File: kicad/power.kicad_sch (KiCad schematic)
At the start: 76 parts, among them U1 MIMXRT1171DVMAB, U8 TPS62086, U9 TPS62825, Y3 24MHz, Y4 32.768kHz

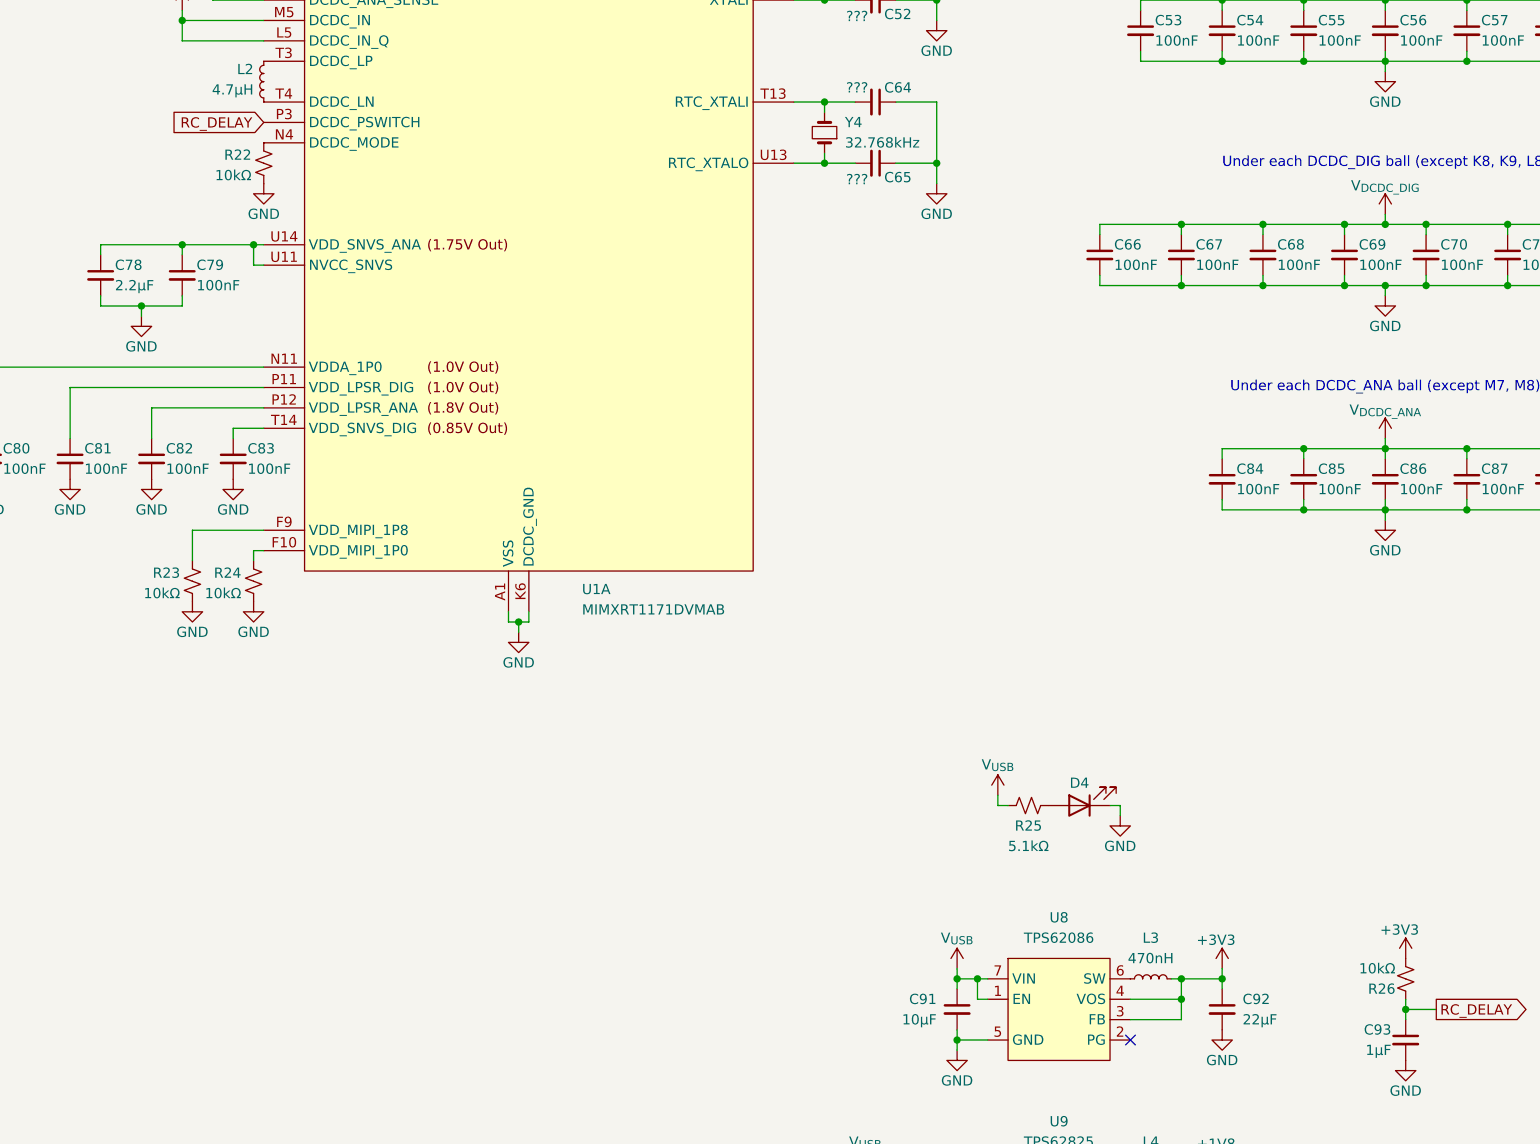
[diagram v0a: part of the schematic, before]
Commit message: added several footprints
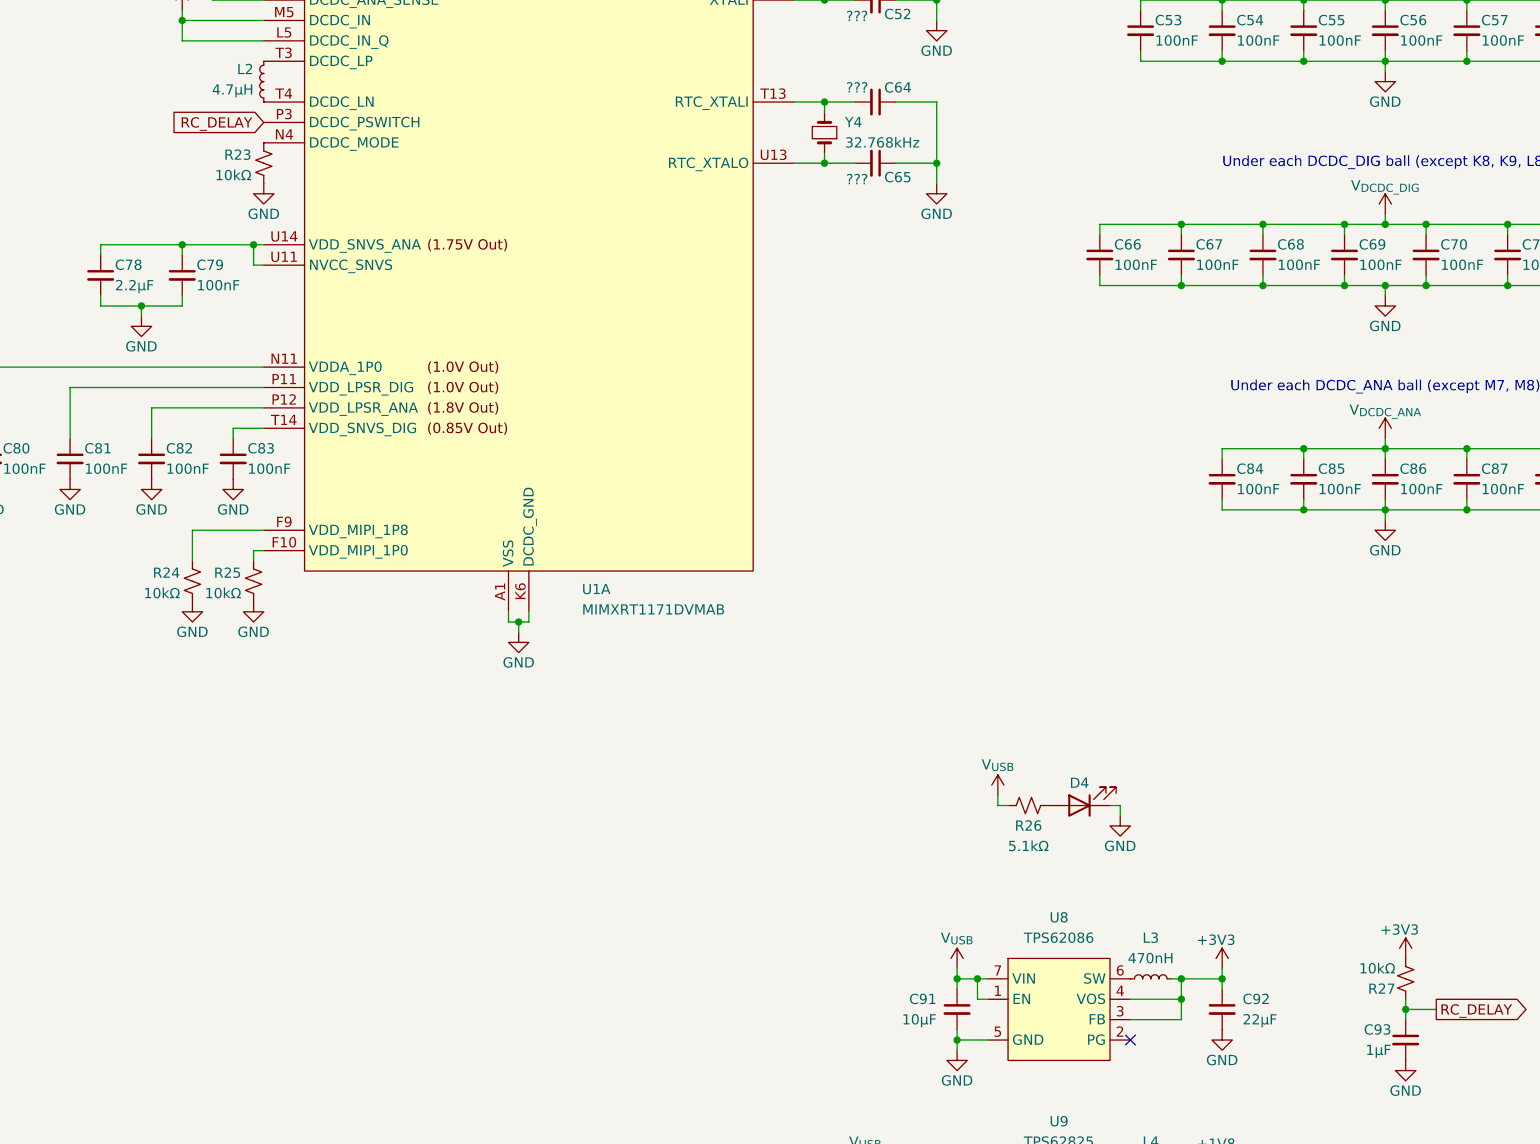
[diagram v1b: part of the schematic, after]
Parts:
- C37, C38, C39, C40, C41, C42, C43, C44, C45, C46, C53, C54, C55, C56, C57, C58, C59, C66, C67, C68, C69, C70, C71, C72, C73, C79, C80, C81, C82, C83, C84, C85, C86, C87, C88: footprint (none) -> Capacitor_SMD:C_0201_0603Metric
- C47, C48, C49, C50, C60, C61, C62, C63, C74, C75, C76, C77, C89, C90, C91: footprint (none) -> Capacitor_SMD:C_0402_1005Metric
- D4: footprint (none) -> LED_SMD:LED_0603_1608Metric
- R23: renamed from R22; footprint (none) -> Resistor_SMD:R_0201_0603Metric
- R24: renamed from R23; footprint (none) -> Resistor_SMD:R_0201_0603Metric
- R25: renamed from R24; footprint (none) -> Resistor_SMD:R_0201_0603Metric
- R26: renamed from R25; footprint (none) -> Resistor_SMD:R_0201_0603Metric
- R27: renamed from R26; footprint (none) -> Resistor_SMD:R_0201_0603Metric
- U1: footprint Package_BGA:MAPBGA-289_14x14mm_Layout17x17_P0.8mm -> project_footprints:MIMXRT1171DVMAB
- U8: footprint (none) -> project_footprints:TPS62086
- U9: footprint (none) -> project_footprints:TPS62825

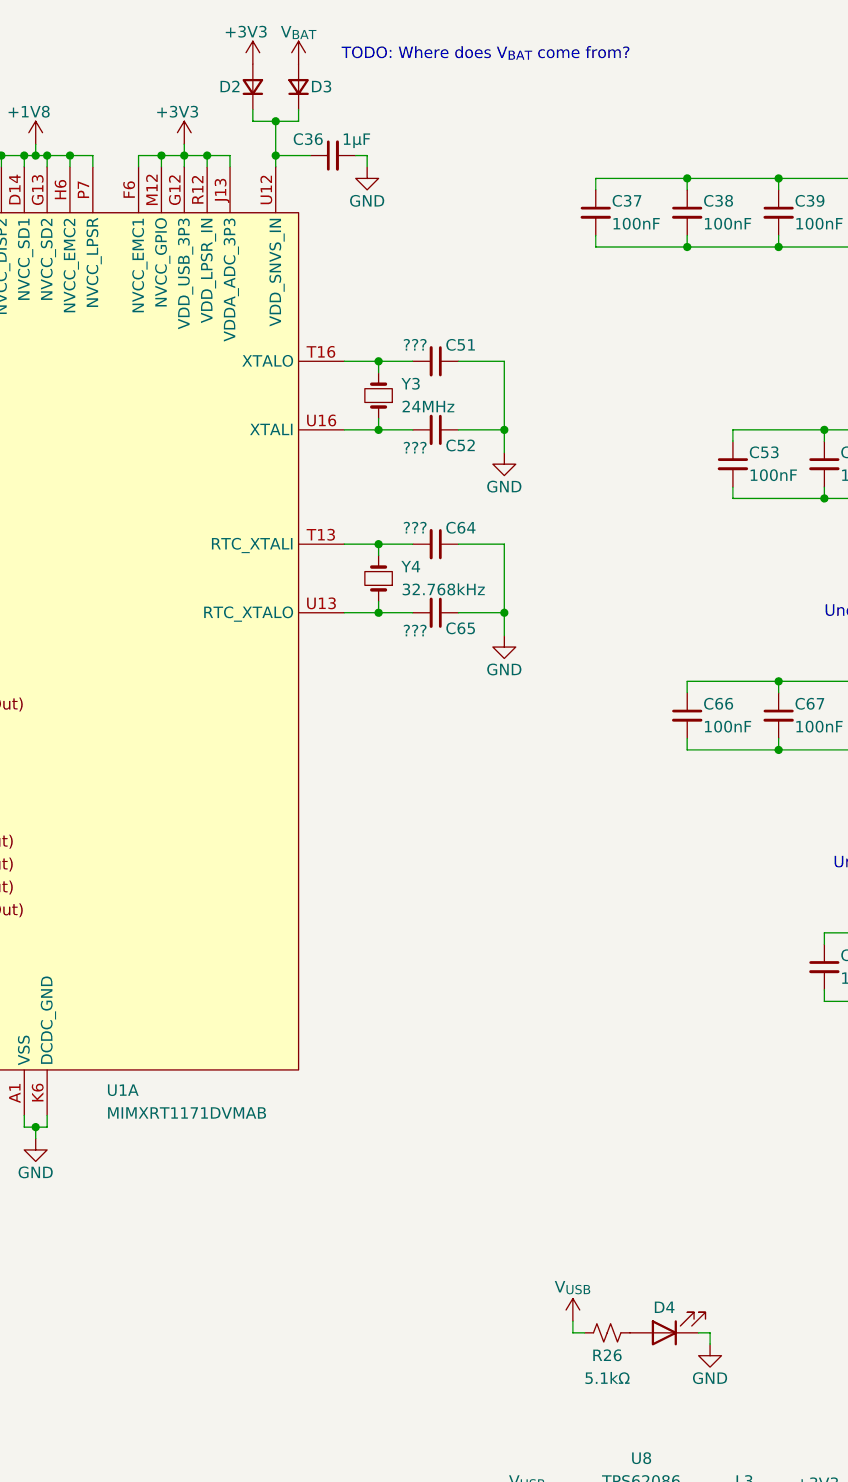
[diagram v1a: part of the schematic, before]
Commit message: added RTC battery connector
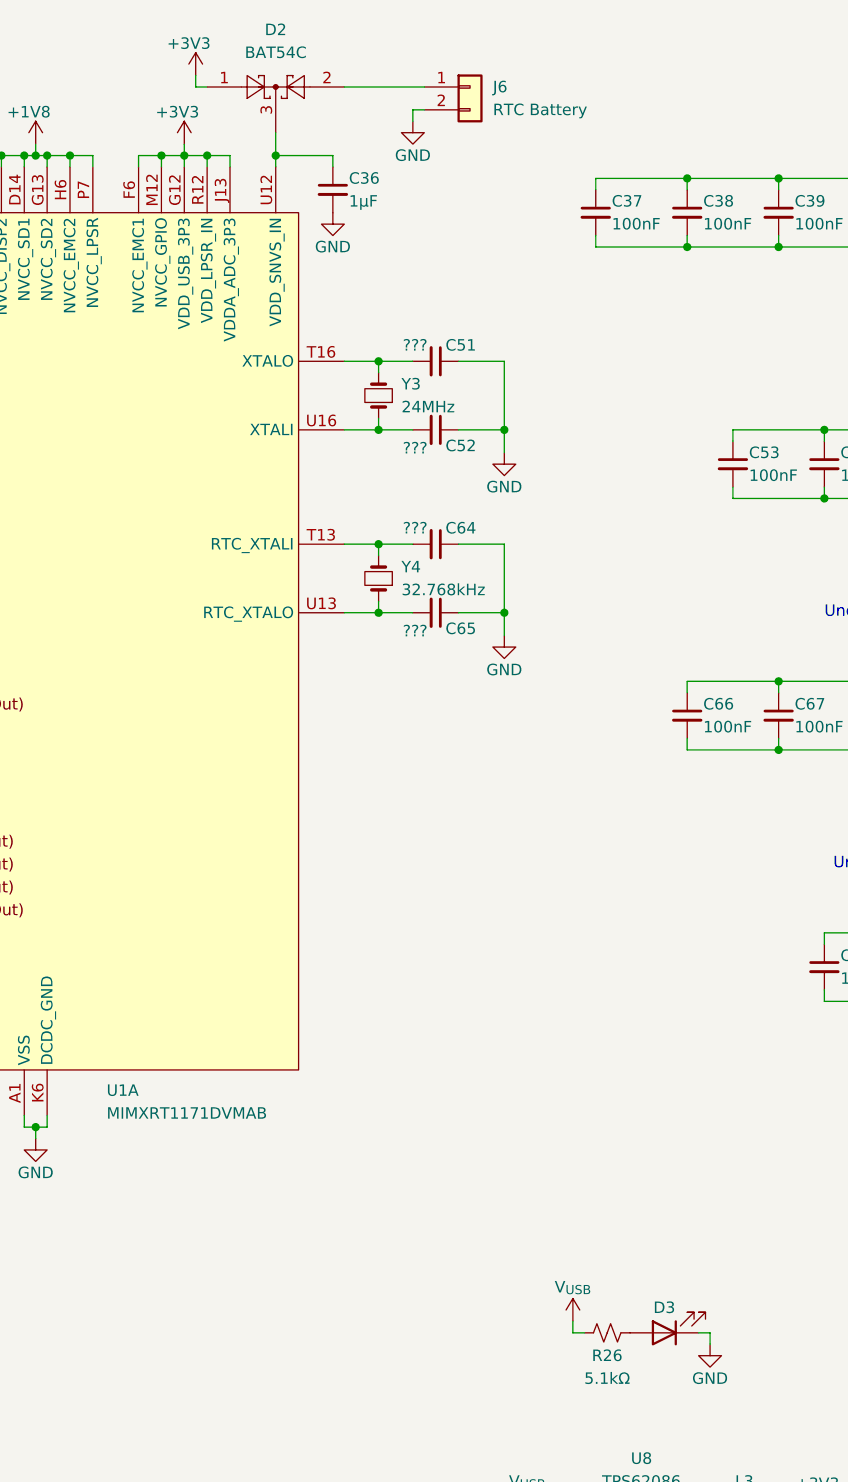
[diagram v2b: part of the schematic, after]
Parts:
- removed D2, D3: ???, symbol Device:D_Small
- added D2: BAT54C, Package_TO_SOT_SMD:SOT-23, symbol Diode:BAT54C
- added J6: RTC Battery, project_footprints:Header-1x02, symbol Connector_Generic:Conn_01x02
- C36: footprint (none) -> Capacitor_SMD:C_0402_1005Metric
- renumbered D4 to D3
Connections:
- net +3V3: now also D2.1
- net GND: now also J6.2 (Pin_2)
- net at C36.1, U1.U12 (VDD_SNVS_IN): now also D2.3
- new net: D2.2, J6.1 (Pin_1)
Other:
- note removed: "TODO: Where does V_{BAT} come from?"

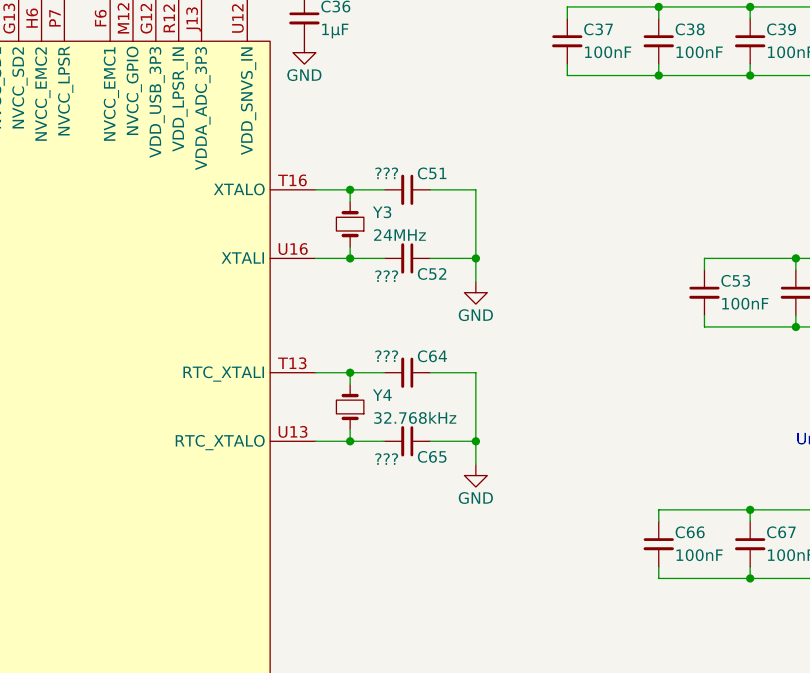
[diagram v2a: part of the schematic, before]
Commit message: added crystal footprints
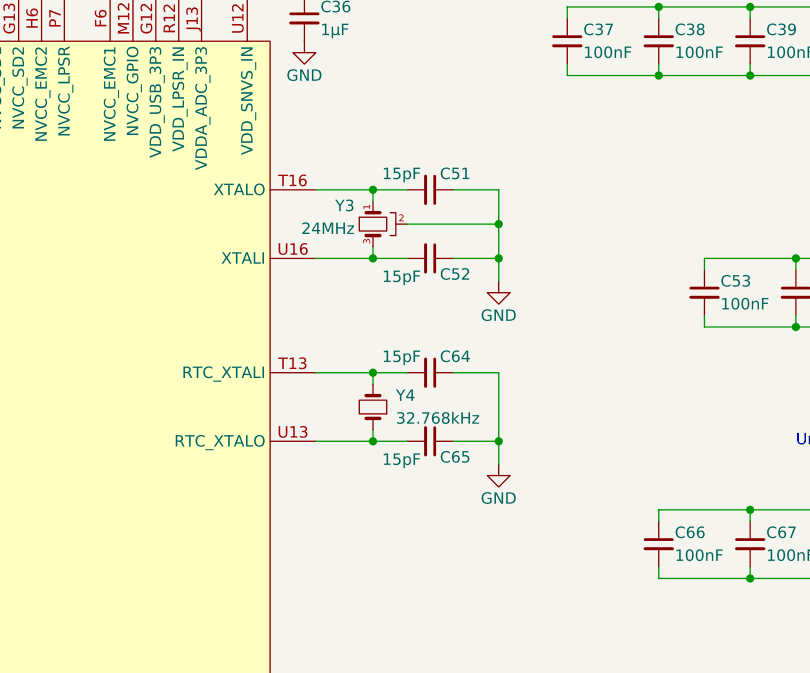
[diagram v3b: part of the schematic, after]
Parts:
- removed Y3: 24MHz, symbol Device:Crystal_Small
- added Y3: 24MHz, project_footprints:Crystal-4-Pin, symbol project_symbols:Crystal_GND24_Small
- C51, C52, C64, C65: value ??? -> 15pF; footprint (none) -> Capacitor_SMD:C_0402_1005Metric
- Y4: footprint (none) -> project_footprints:Crystal-2-Pin
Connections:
- net GND: now also Y3.2 (GND), Y3.4 (GND)
- net at C51.2, U1.T16 (XTALO): now also Y3.1
- net at C52.2, U1.U16 (XTALI): now also Y3.3
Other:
- moved on the sheet: C51, C52, Y4
